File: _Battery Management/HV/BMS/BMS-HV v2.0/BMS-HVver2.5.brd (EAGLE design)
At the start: 152.4 x 124.8 mm, 428 parts, among them J3 M2S02B-PASK-2(LF)(SN), J4 M2S02B-PASK-2(LF)(SN), Q1 BSS308PE, Q10 BSS308PE, Q11 BSS308PE, Q12 BSS308PE, Q13 BSS308PE, Q14 BSS308PE, Q15 BSS308PE, Q16 BSS308PE, Q17 BSS308PE, Q18 BSS308PE, Q19 BSS308PE, Q2 BSS308PE, Q20 BSS308PE, Q21 BSS308PE, Q22 BSS308PE, Q23 BSS308PE, Q24 BSS308PE, Q25 BSS308PE, Q26 BSS308PE, Q27 BSS308PE, Q28 BSS308PE, Q29 BSS308PE, Q3 BSS308PE, Q30 BSS308PE, Q31 BSS308PE, Q32 BSS308PE, Q33 BSS308PE, Q34 BSS308PE, Q35 BSS308PE, Q36 BSS308PE, Q37 BSS308PE, Q38 BSS308PE, Q39 BSS308PE, Q4 BSS308PE, Q5 BSS308PE, Q6 BSS308PE, Q7 BSS308PE, Q8 BSS308PE, Q9 BSS308PE, U1 LTC6804-2, U2 LTC6804-2, U3 LTC6804-2

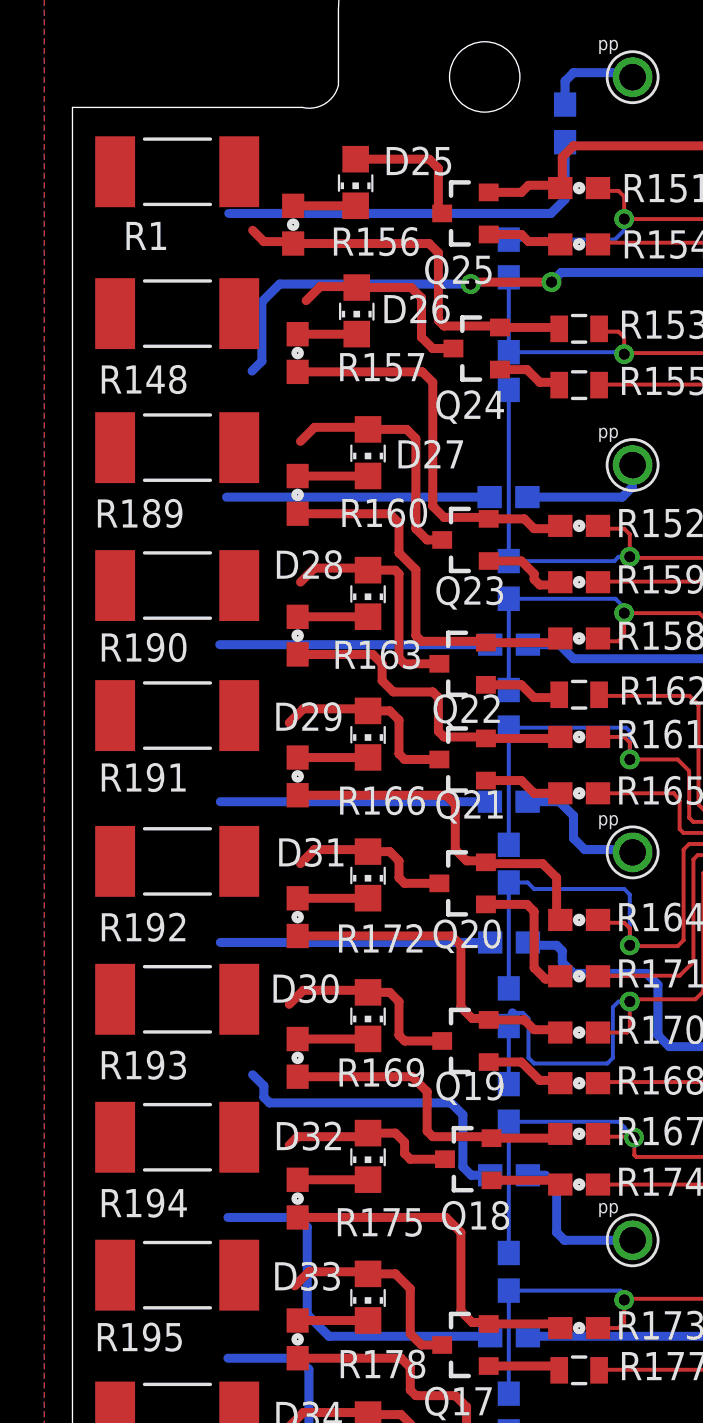
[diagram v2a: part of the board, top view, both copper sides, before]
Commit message: 
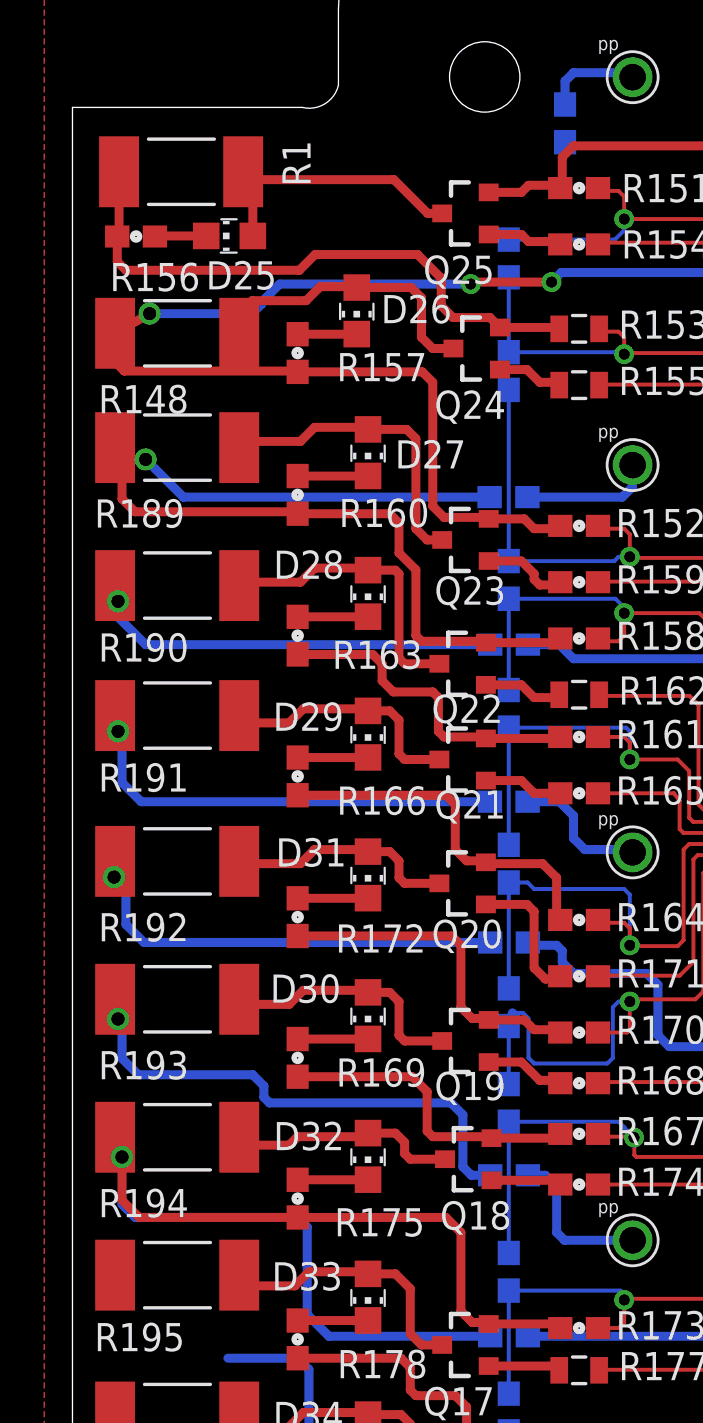
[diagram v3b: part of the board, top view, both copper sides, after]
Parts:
- moved R156 7.11 mm to (-73.3, 36.6), turned to 0 degrees
- moved D25 6.18 mm to (-69.1, 36.6), turned to 90 degrees
- moved R148 0.89 mm to (-71.5, 32.2)
- moved R1 0.18 mm to (-71.3, 39.5)
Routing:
- net N$86: track 32.5 -> 52.8 mm, vias 0 -> 1
- net N$66: track 28.9 -> 45.3 mm, vias 0 -> 1
- net N$62: track 45.5 -> 60.8 mm, vias 2 -> 3
- net N$82: track 28.5 -> 37.5 mm, vias 0 -> 1
- net N$58: track 35.5 -> 26.9 mm
- net N$77: track 28.7 -> 36.6 mm, vias 0 -> 1
- net N$81: track 27.6 -> 35.3 mm, vias 0 -> 1
- net N$70: track 27.1 -> 33.7 mm, vias 0 -> 1
- net N$56: track 6.06 -> 12.3 mm
- net N$60: track 9.11 -> 13.1 mm
- net N$64: track 11.1 -> 14.0 mm
- net N$68: track 10.5 -> 13.4 mm
- net N$79: track 7.61 -> 10.4 mm
- net N$88: track 9.47 -> 12.2 mm
- net N$84: track 8.04 -> 10.4 mm
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
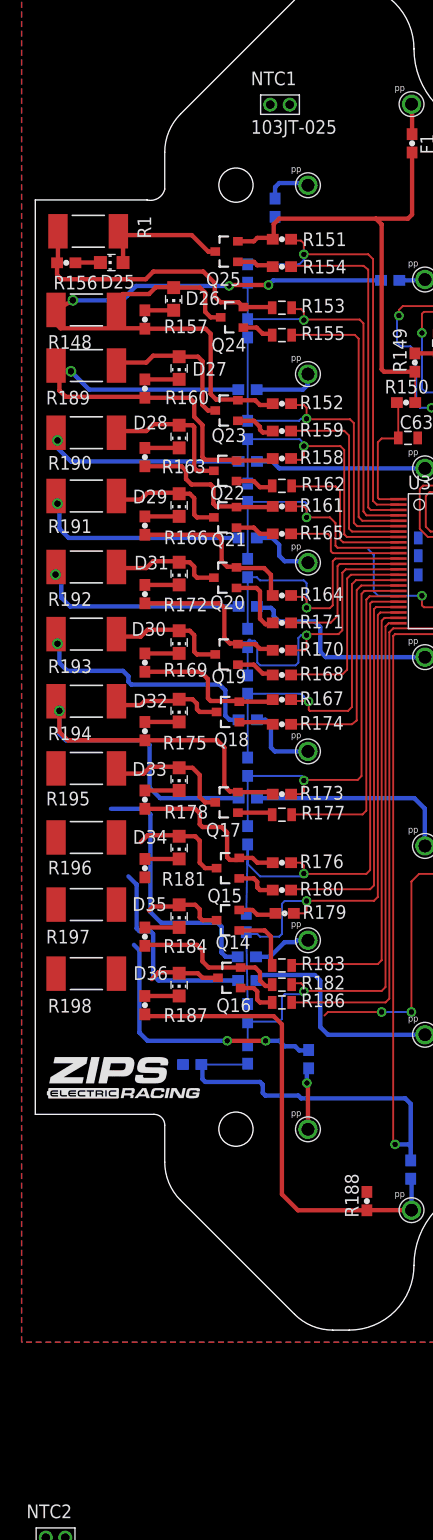
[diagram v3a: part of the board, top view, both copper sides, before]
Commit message: 
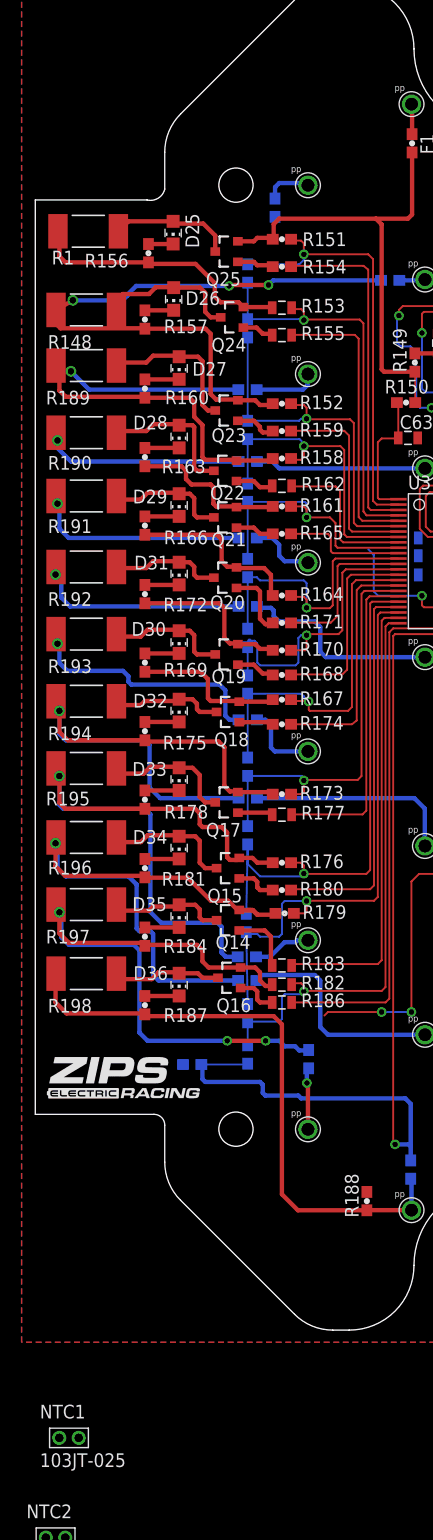
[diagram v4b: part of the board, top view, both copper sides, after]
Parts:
- moved NTC1 125.1 mm to (-73.1, -72.4)
- moved R156 7.67 mm to (-65.7, 37.4), turned to 90 degrees
- moved D25 6.33 mm to (-63.4, 39.3), turned to 180 degrees
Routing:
- net N$94: track 22.5 -> 54.8 mm, vias 0 -> 1
- net N$106: track 39.4 -> 59.1 mm, vias 2 -> 3
- net N$90: track 40.3 -> 58.5 mm, vias 0 -> 1
- net N$105: track 44.5 -> 57.2 mm
- net N$96: track 7.53 -> 11.3 mm
- net N$101: track 6.61 -> 10.1 mm
- net N$92: track 9.74 -> 12.2 mm
- net N$58: track 26.9 -> 25.1 mm
- net N$56: track 12.3 -> 11.4 mm
